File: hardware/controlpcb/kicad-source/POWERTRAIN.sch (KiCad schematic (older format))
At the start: 53 parts, among them P2 WR-TBL_691313710002, P3 WR-TBL_691313710002, U10 IFX007T, U11 OPA2374AIDCN, U12 IFX007T, U13 IFX007T, U14 74xx08, U8 OPA2374AIDCN, U9 IFX007T

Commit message: added kicad source
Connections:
- net BEMF1 renamed DRIVE_BEMF1
- net BEMF2 renamed DRIVE_BEMF2
- net INH renamed DRIVE_INH
- net IS1 renamed DRIVE_IS
- net PWM1 renamed DRIVE_PWM1
- net PWM2 renamed DRIVE_PWM2
- net PWM3 renamed DRIVE_PWM3
- net PWM4 renamed DRIVE_PWM4
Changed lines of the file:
@@
 SENSE_B
 Text GLabel 1200 1700 0    50   Input ~ 0
-INH
+DRIVE_INH
 Text GLabel 1250 3550 0    50   Input ~ 0
-INH
+DRIVE_INH
 Wire Wire Line
 	1350 1700 1200 1700
@@
 SENSE_A
 Text GLabel 6500 1700 0    50   Input ~ 0
-INH
+DRIVE_INH
 Text GLabel 6550 3550 0    50   Input ~ 0
-INH
+DRIVE_INH
 Wire Wire Line
 	6650 1700 6500 1700
@@
 	4600 6750 4800 6750
 Text GLabel 7050 5050 2    50   Output ~ 0
-BEMF1
+DRIVE_BEMF1
 Text Label 3500 6800 0    50   ~ 0
 VREF_B
@@
 Measure up to about 5V
 Text GLabel 3450 5100 2    50   Output ~ 0
-BEMF2
+DRIVE_BEMF2
 Wire Wire Line
 	2750 5100 3450 5100
@@
 change rating for different input
 Text GLabel 8200 5750 2    50   Output ~ 0
-IS1
+DRIVE_IS
 $Comp
 L devices:R_0603 R40
@@
 $EndComp
 Text GLabel 9500 5050 0    50   Input ~ 0
-PWM1
+DRIVE_PWM1
 Text GLabel 9500 5250 0    50   Input ~ 0
-PWM2
+DRIVE_PWM2
 Text GLabel 9500 5450 0    50   Input ~ 0
-PWM3
+DRIVE_PWM3
 Text GLabel 9500 5650 0    50   Input ~ 0
-PWM4
+DRIVE_PWM4
 Wire Wire Line
 	9500 5050 9750 5050

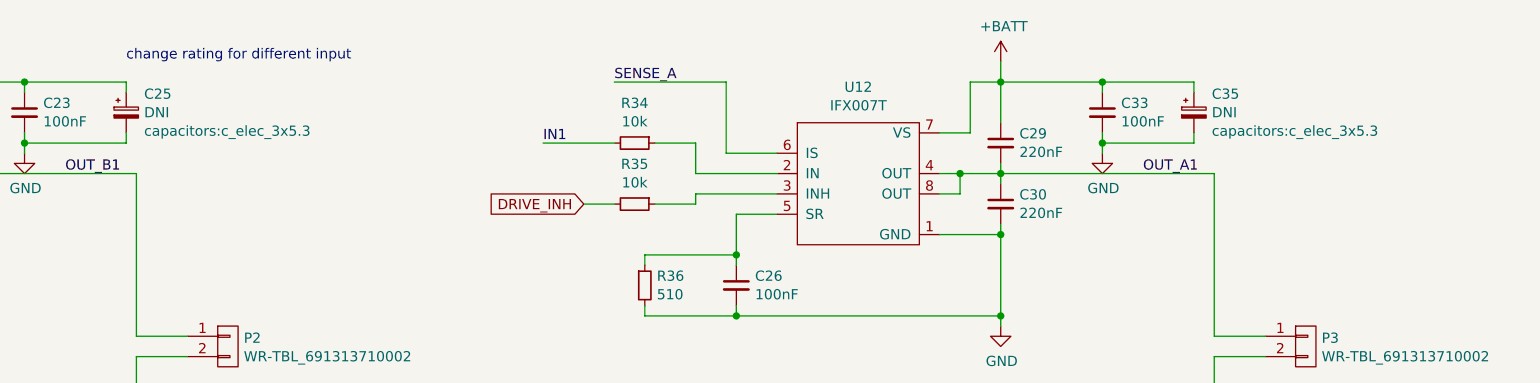
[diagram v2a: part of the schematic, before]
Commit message: added servo connector
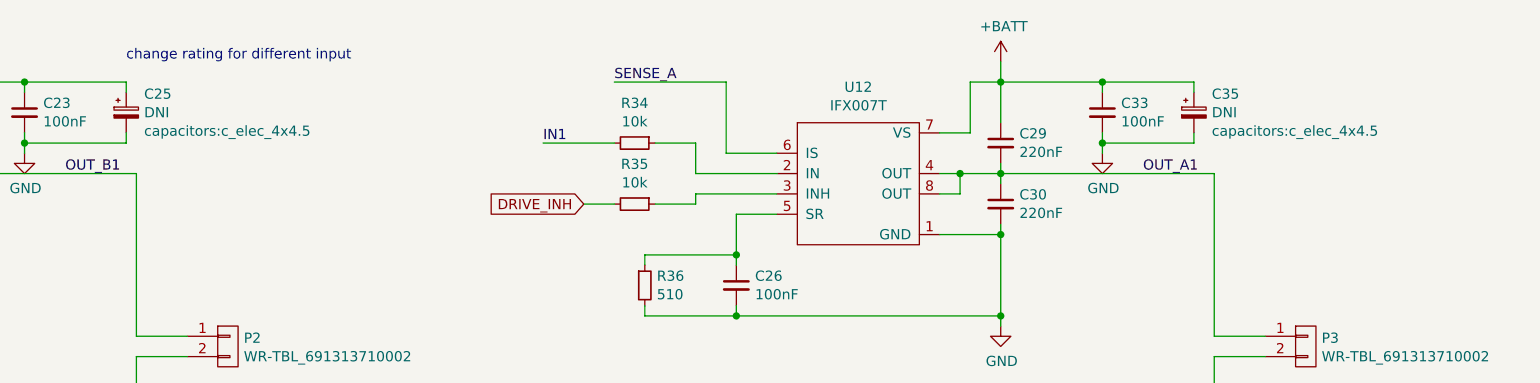
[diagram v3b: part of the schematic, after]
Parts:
- C25, C35: footprint capacitors:c_elec_3x5.3 -> capacitors:c_elec_4x4.5
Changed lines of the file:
@@
 F 0 "C25" H 4338 1341 50  0000 L CNN
 F 1 "DNI" H 4338 1250 50  0000 L CNN
-F 2 "capacitors:c_elec_3x5.3" H 4338 1159 50  0000 L CNN
+F 2 "capacitors:c_elec_4x4.5" H 4338 1159 50  0000 L CNN
 F 3 "" H 4250 1250 50  0000 C CNN
 	1    4250 1250
@@
 F 0 "C35" H 9588 1341 50  0000 L CNN
 F 1 "DNI" H 9588 1250 50  0000 L CNN
-F 2 "capacitors:c_elec_3x5.3" H 9588 1159 50  0000 L CNN
+F 2 "capacitors:c_elec_4x4.5" H 9588 1159 50  0000 L CNN
 F 3 "" H 9500 1250 50  0000 C CNN
 	1    9500 1250
